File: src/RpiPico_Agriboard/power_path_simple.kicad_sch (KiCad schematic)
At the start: 7 parts, among them Q12 BSP170P-VB, Q13 BSP170P-VB

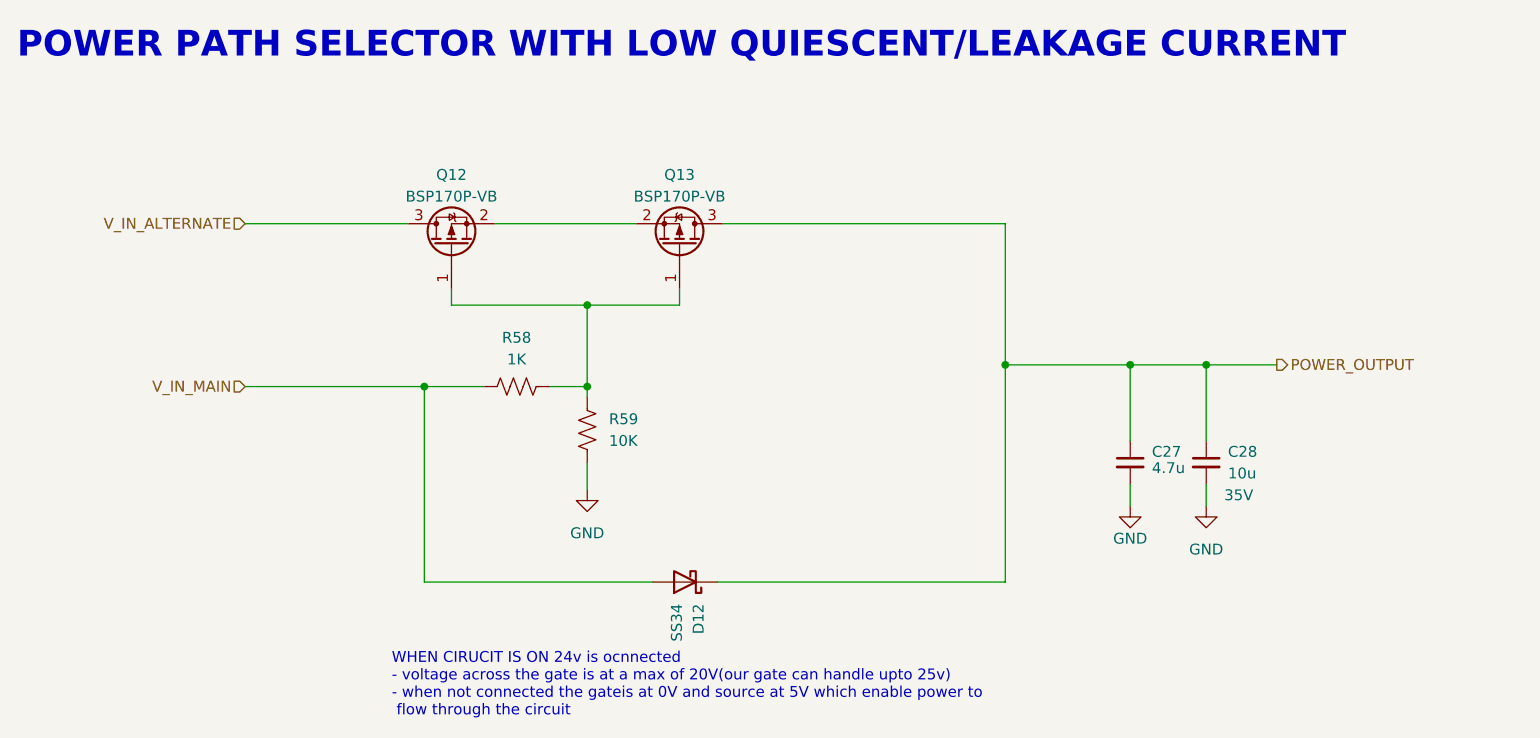
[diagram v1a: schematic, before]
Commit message: complete board update and routing
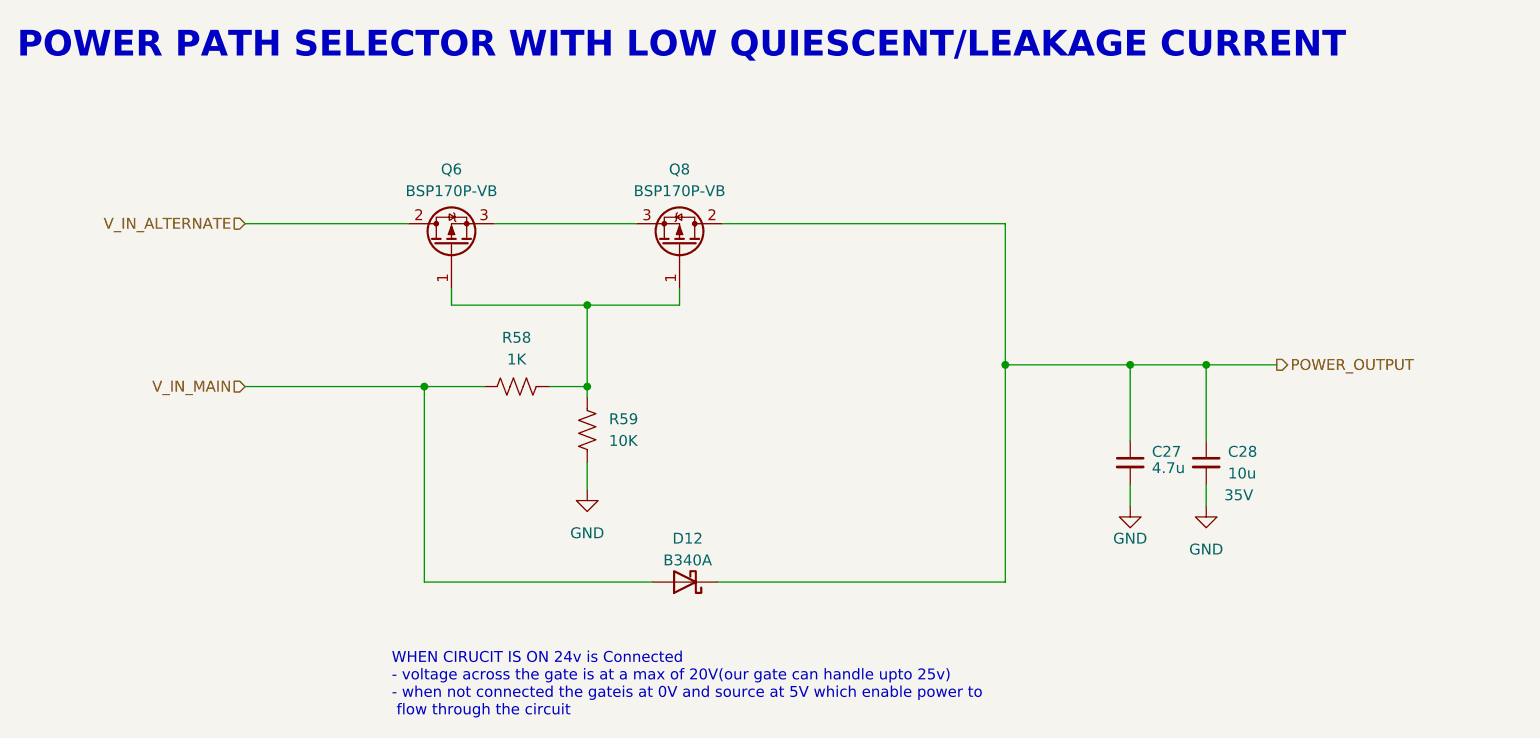
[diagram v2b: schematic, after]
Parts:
- removed Q12, Q13: BSP170P-VB, Package_TO_SOT_SMD:SOT-223-3_TabPin2, symbol Device:Q_PMOS_GSD
- added Q6, Q8: BSP170P-VB, Package_TO_SOT_SMD:SOT-223-3_TabPin2, symbol Device:Q_PMOS_GDS
- D12: value SS34 -> B340A
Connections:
- net POWER_OUTPUT: now also Q8.2 (D)
- net V_IN_ALTERNATE: now also Q6.2 (D)
- net at R58.2, R59.1: now also Q6.1 (G), Q8.1 (G)
- new net: Q6.3 (S), Q8.3 (S)
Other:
- note added: "WHEN CIRUCIT IS ON 24v is Connected - voltage across the gate is at a max of 20V(our gate can handle upto 25v) - when not connected the gateis at 0V and source at 5V which enable power to flow through the circuit"
- note removed: "WHEN CIRUCIT IS ON 24v is ocnnected - voltage across the gate is at a max of 20V(our gate can handle upto 25v) - when not connected the gateis at 0V and source at 5V which enable power to flow through the circuit"
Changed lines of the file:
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@@
     (effects (font (size 3 3) bold) (justify left bottom))
   )
-  (text "WHEN CIRUCIT IS ON 24v is ocnnected\n- voltage across the gate is at a max of 20V(our gate can handle upto 25v)\n- when not connected the gateis at 0V and source at 5V which enable power to\n flow through the circuit"
+  (text "WHEN CIRUCIT IS ON 24v is Connected\n- voltage across the gate is at a max of 20V(our gate can handle upto 25v)\n- when not connected the gateis at 0V and source at 5V which enable power to\n flow through the circuit"
     (at 120.015 132.715 0)
     (effects (font (size 1.27 1.27)) (justify left bottom))
@@
     (effects (font (size 1.27 1.27)) (justify right))
   )
-  (symbol (lib_id "Device:Q_PMOS_GSD") (at 127 77.47 90) (unit 1)
-    (in_bom yes) (on_board yes) (dnp no) (fields_autoplaced)
-    (property "Reference" "Q12" (at 127 69.215 90)
-      (effects (font (size 1.27 1.27)))
-    )
-    (property "Value" "BSP170P-VB" (at 127 71.755 90)
-      (effects (font (size 1.27 1.27)))
-    )
-    (property "Footprint" "Package_TO_SOT_SMD:SOT-223-3_TabPin2" (at 124.46 72.39 0)
-      (effects (font (size 1.27 1.27)) hide)
-    )
-    (property "Datasheet" "~" (at 127 77.47 0)
-      (effects (font (size 1.27 1.27)) hide)
-    )
-    (pin "1")
-    (pin "2")
-    (pin "3")
-    (instances
-      (project "Weather_Station_Project"
-        (path "/aaf5c359-cd8c-4cad-b3ec-83c1a2a58ae1/5c9d2896-d12c-4a54-8123-892fb6342e25/eea1e41a-274e-4930-b57c-69d99ff42c09/705d5845-37bb-48c7-9641-198316a19ba9"
-          (reference "Q12") (unit 1)
-        )
-      )
-      (project "RpiPico_Agriboard"
-        (path "/c2474b65-c0e8-4987-86b2-fddddd4113dc/f3a00526-8108-483c-9ec5-d5fcf6fe065b/e1b77c03-2b38-43f3-998b-3c2f1972d847"
-          (reference "Q6") (unit 1)
-        )
-      )
-    )
-  )
   (symbol (lib_id "Device:C_Small") (at 206.375 102.87 0) (unit 1)
     (in_bom yes) (on_board yes) (dnp no)
@@
   (symbol (lib_id "Device:D_Schottky") (at 154.305 116.84 180) (unit 1)
     (in_bom yes) (on_board yes) (dnp no) (fields_autoplaced)
-    (property "Reference" "D12" (at 155.8926 119.38 90)
-      (effects (font (size 1.27 1.27)) (justify left))
-    )
-    (property "Value" "SS34" (at 153.3526 119.38 90)
-      (effects (font (size 1.27 1.27)) (justify left))
+    (property "Reference" "D12" (at 154.6225 111.76 0)
+      (effects (font (size 1.27 1.27)))
+    )
+    (property "Value" "B340A" (at 154.6225 114.3 0)
+      (effects (font (size 1.27 1.27)))
     )
     (property "Footprint" "Diode_SMD:D_SMA" (at 154.305 116.84 0)
@@
     )
   )
+  (symbol (lib_id "Device:Q_PMOS_GDS") (at 153.67 77.47 270) (mirror x) (unit 1)
+    (in_bom yes) (on_board yes) (dnp no)
+    (property "Reference" "Q8" (at 153.67 68.58 90)
+      (effects (font (size 1.27 1.27)))
+    )
+    (property "Value" "BSP170P-VB" (at 153.67 71.12 90)
+      (effects (font (size 1.27 1.27)))
+    )
+    (property "Footprint" "Package_TO_SOT_SMD:SOT-223-3_TabPin2" (at 156.21 72.39 0)
+      (effects (font (size 1.27 1.27)) hide)
+    )
+    (property "Datasheet" "~" (at 153.67 77.47 0)
+      (effects (font (size 1.27 1.27)) hide)
+    )
+    (pin "1")
+    (pin "2")
+    (pin "3")
+    (instances
+      (project "RpiPico_Agriboard"
+        (path "/c2474b65-c0e8-4987-86b2-fddddd4113dc/f3a00526-8108-483c-9ec5-d5fcf6fe065b/e1b77c03-2b38-43f3-998b-3c2f1972d847"
+          (reference "Q8") (unit 1)
+        )
+      )
+    )
+  )
   (symbol (lib_id "power:GND") (at 215.265 107.95 0) (unit 1)
     (in_bom yes) (on_board yes) (dnp no)
@@
     )
   )
-  (symbol (lib_id "Device:Q_PMOS_GSD") (at 153.67 77.47 270) (mirror x) (unit 1)
-    (in_bom yes) (on_board yes) (dnp no) (fields_autoplaced)
-    (property "Reference" "Q13" (at 153.67 69.215 90)
-      (effects (font (size 1.27 1.27)))
-    )
-    (property "Value" "BSP170P-VB" (at 153.67 71.755 90)
-      (effects (font (size 1.27 1.27)))
-    )
-    (property "Footprint" "Package_TO_SOT_SMD:SOT-223-3_TabPin2" (at 156.21 72.39 0)
-      (effects (font (size 1.27 1.27)) hide)
-    )
-    (property "Datasheet" "~" (at 153.67 77.47 0)
+  (symbol (lib_id "Device:Q_PMOS_GDS") (at 127 77.47 90) (unit 1)
+    (in_bom yes) (on_board yes) (dnp no) (fields_autoplaced)
+    (property "Reference" "Q6" (at 127 68.58 90)
+      (effects (font (size 1.27 1.27)))
+    )
+    (property "Value" "BSP170P-VB" (at 127 71.12 90)
+      (effects (font (size 1.27 1.27)))
+    )
+    (property "Footprint" "Package_TO_SOT_SMD:SOT-223-3_TabPin2" (at 124.46 72.39 0)
+      (effects (font (size 1.27 1.27)) hide)
+    )
+    (property "Datasheet" "~" (at 127 77.47 0)
       (effects (font (size 1.27 1.27)) hide)
     )
@@
     (pin "3")
     (instances
-      (project "Weather_Station_Project"
-        (path "/aaf5c359-cd8c-4cad-b3ec-83c1a2a58ae1/5c9d2896-d12c-4a54-8123-892fb6342e25/eea1e41a-274e-4930-b57c-69d99ff42c09/705d5845-37bb-48c7-9641-198316a19ba9"
-          (reference "Q13") (unit 1)
-        )
-      )
-      (project "RpiPico_Agriboard"
-        (path "/c2474b65-c0e8-4987-86b2-fddddd4113dc/f3a00526-8108-483c-9ec5-d5fcf6fe065b/e1b77c03-2b38-43f3-998b-3c2f1972d847"
-          (reference "Q8") (unit 1)
-        )
-      )
+      (project "RpiPico_Agriboard"
+        (path "/c2474b65-c0e8-4987-86b2-fddddd4113dc/f3a00526-8108-483c-9ec5-d5fcf6fe065b/e1b77c03-2b38-43f3-998b-3c2f1972d847"
+          (reference "Q6") (unit 1)
+        )
+      )
